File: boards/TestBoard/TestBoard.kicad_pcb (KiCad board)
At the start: 2 copper layers, 27 x 69 mm, 26 parts, among them J1 Conn_01x04, J10 Conn_01x02, J11 Conn_01x02, J2 Conn_01x04, J3 Conn_01x80, J4 Conn_01x02, J5 Conn_01x80, U1 MCP23017_ML, U2 MCP23017_ML, U3 MCP23017_ML, U4 MCP23017_ML, U5 MCP23017_ML

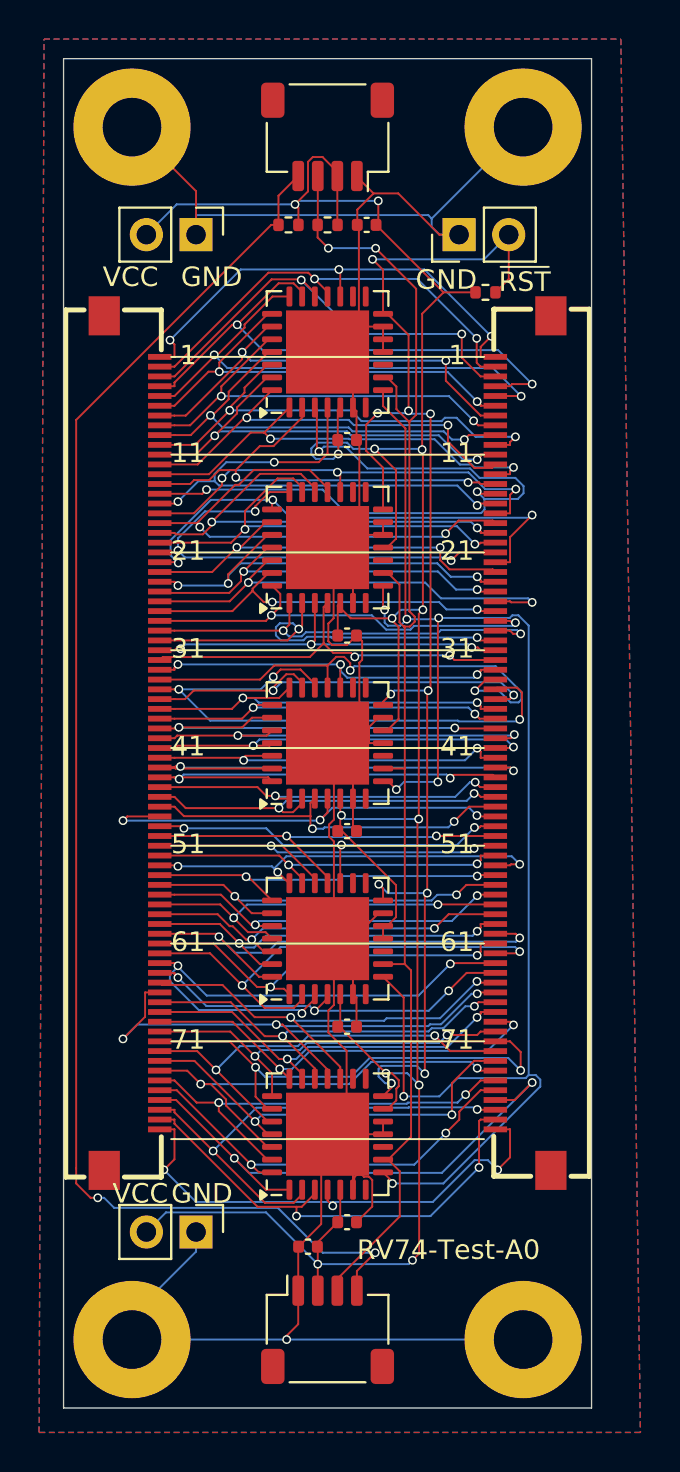
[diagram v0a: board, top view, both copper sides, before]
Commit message: Re-route with wider tracks and vias, to avoid "Danger" notifications from JLCPCB.
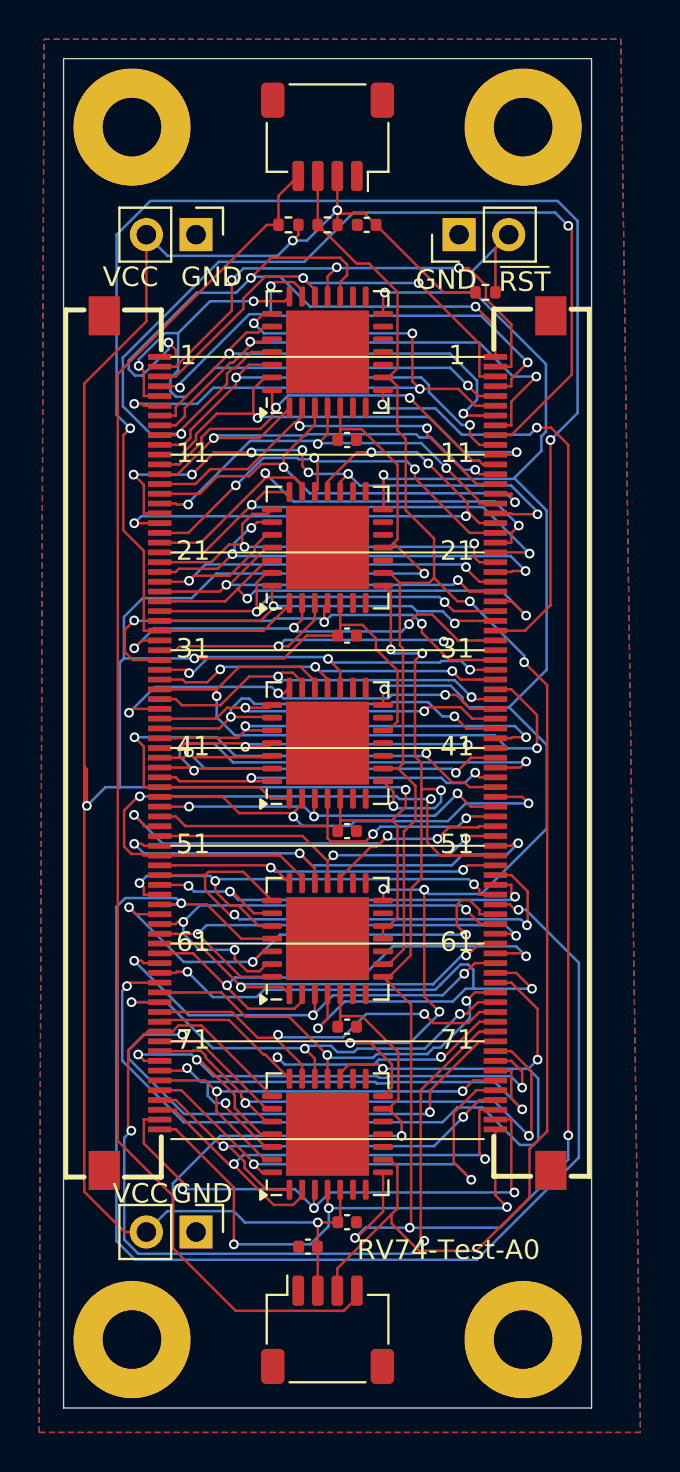
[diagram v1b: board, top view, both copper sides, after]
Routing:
- net GND: track 162.7 -> 0.00 mm, vias 1 -> 0
- net VCC: track 151.8 -> 207.9 mm, vias 13 -> 8
- net /A28: track 21.8 -> 77.5 mm
- net /A56: track 20.1 -> 70.0 mm
- net /A8: track 22.9 -> 53.0 mm
- net SDA: track 72.1 -> 101.2 mm
- net /A69: track 20.6 -> 48.0 mm
- net /A64: track 23.0 -> 49.5 mm, vias 2 -> 3
- net SCK: track 81.4 -> 106.6 mm, vias 7 -> 9
- net /A51: track 18.9 -> 34.0 mm
- net ~{RESET}: track 72.7 -> 87.6 mm, vias 10 -> 7
- net /A63: track 20.0 -> 34.3 mm
- net /A44: track 18.6 -> 30.2 mm
- net /A0: track 24.5 -> 35.6 mm
- net /A14: track 35.5 -> 24.6 mm, vias 3 -> 2
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
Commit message: Use larger vias. Auto-routing is still working !! That's good placement :)
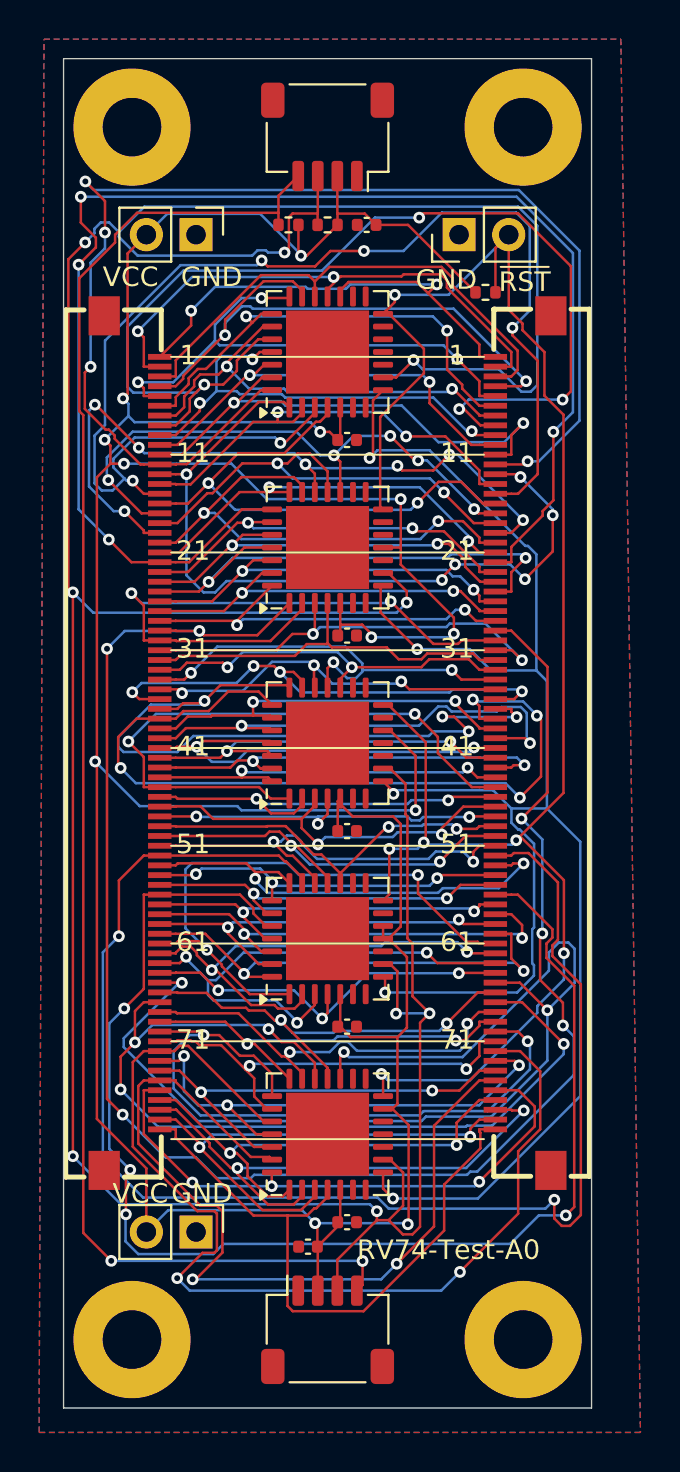
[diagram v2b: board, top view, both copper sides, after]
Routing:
- net SDA: track 101.2 -> 182.3 mm, vias 2 -> 9
- net /A21: track 21.3 -> 73.1 mm, vias 2 -> 4
- net /A56: track 70.0 -> 19.8 mm
- net /A55: track 24.6 -> 69.2 mm, vias 3 -> 4
- net /A11: track 21.4 -> 65.6 mm, vias 2 -> 4
- net /A14: track 24.6 -> 65.8 mm, vias 2 -> 5
- net /A51: track 34.0 -> 73.8 mm
- net /A7: track 27.1 -> 56.4 mm, vias 2 -> 4
- net /A8: track 53.0 -> 24.0 mm, vias 2 -> 3
- net /A71: track 28.4 -> 53.4 mm
- net /A37: track 19.2 -> 42.1 mm, vias 2 -> 4
- net /A66: track 24.0 -> 46.8 mm, vias 3 -> 4
- net /A74: track 22.5 -> 44.3 mm
- net /A12: track 23.4 -> 39.9 mm, vias 2 -> 6
- net /A36: track 22.2 -> 38.1 mm, vias 3 -> 4
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
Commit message: EVen larger vias and track clearance
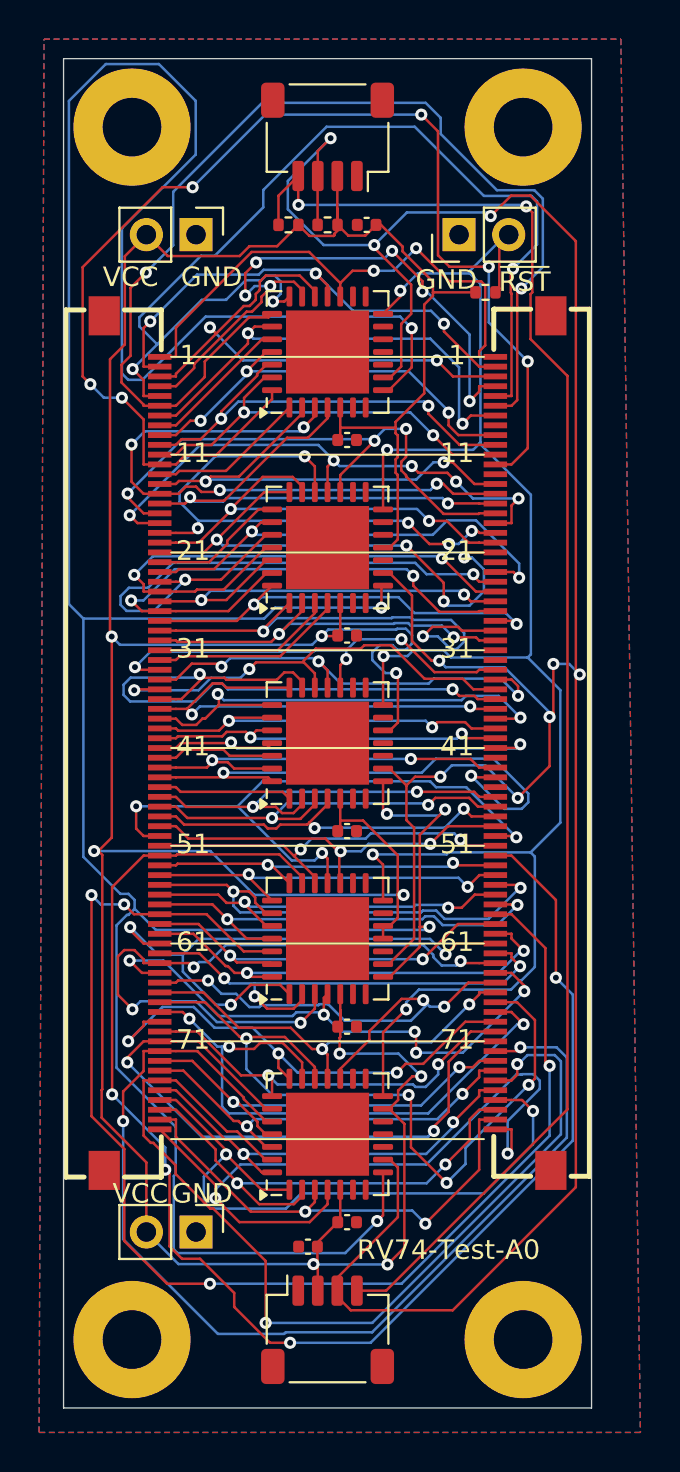
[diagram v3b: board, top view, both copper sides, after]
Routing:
- net SCK: track 94.3 -> 167.6 mm, vias 5 -> 6
- net /A21: track 73.1 -> 6.96 mm, vias 4 -> 0
- net /A28: track 89.3 -> 25.2 mm, vias 6 -> 2
- net /A55: track 69.2 -> 19.8 mm, vias 4 -> 2
- net /A7: track 56.4 -> 7.57 mm, vias 4 -> 0
- net /A57: track 23.2 -> 67.6 mm, vias 2 -> 4
- net /A14: track 65.8 -> 31.8 mm, vias 5 -> 4
- net SDA: track 182.3 -> 148.5 mm
- net /A5: track 24.5 -> 56.9 mm
- net /A12: track 39.9 -> 8.04 mm, vias 6 -> 0
- net /A64: track 56.2 -> 25.9 mm
- net /A4: track 27.6 -> 53.8 mm
- net /A44: track 31.7 -> 6.87 mm, vias 2 -> 0
- net /A37: track 42.1 -> 24.4 mm, vias 4 -> 2
- net /A36: track 38.1 -> 23.4 mm, vias 4 -> 2
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
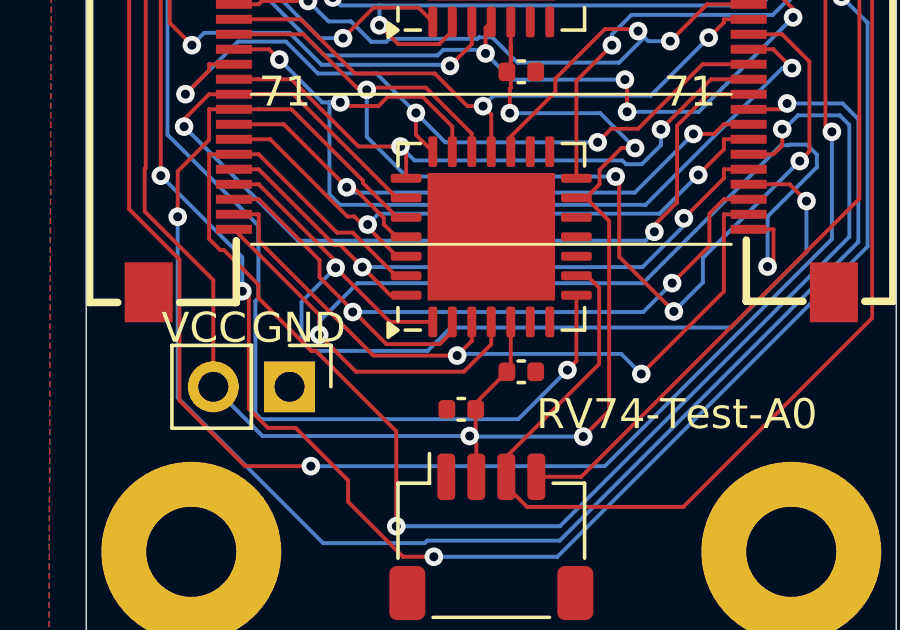
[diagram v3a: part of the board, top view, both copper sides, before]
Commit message: Rework one track to avoid solder-mask / pad clearance violation reported by JLCPCB DFM checker
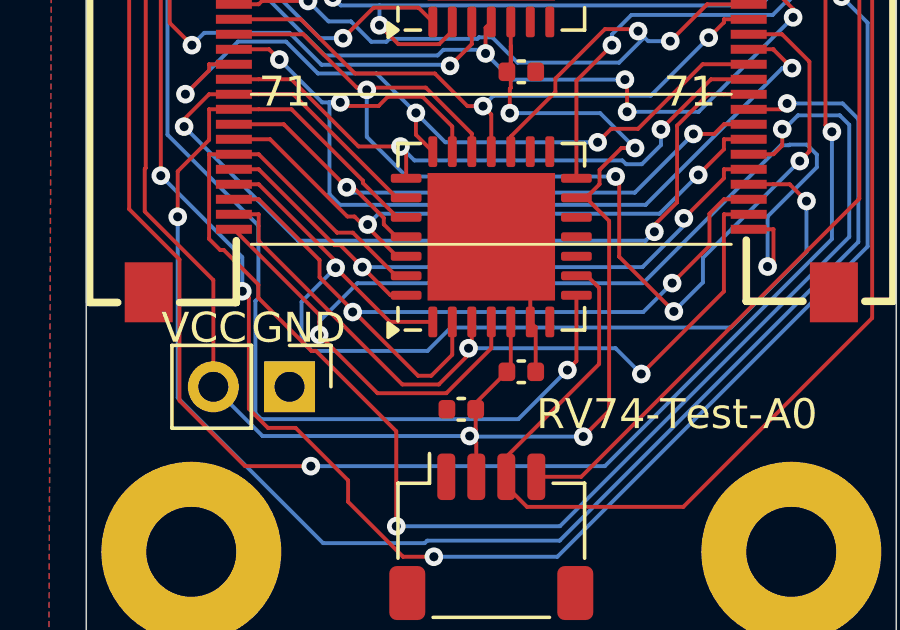
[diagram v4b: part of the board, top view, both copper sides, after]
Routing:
- net GND: track 0.00 -> 5.11 mm
- net /A77: track 25.5 -> 27.2 mm
- net /A78: track 25.0 -> 25.6 mm
- net /A79: track 38.2 -> 38.9 mm
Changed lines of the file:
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@@
 	)
 	(segment
+		(start 140.98 86.5175)
+		(end 140.8 86.3375)
+		(width 0.13)
+		(layer "F.Cu")
+		(net 1)
+	)
+	(segment
+		(start 140.8 86.3375)
+		(end 140.8 84.8)
+		(width 0.13)
+		(layer "F.Cu")
+		(net 1)
+	)
+	(segment
+		(start 140.98 88)
+		(end 140.98 86.5175)
+		(width 0.13)
+		(layer "F.Cu")
+		(net 1)
+	)
+	(segment
+		(start 140.8 84.8)
+		(end 139.5 83.5)
+		(width 0.13)
+		(layer "F.Cu")
+		(net 1)
+	)
+	(segment
 		(start 140.15 78.5357)
 		(end 140.1171 78.5686)
@@
 	)
 	(segment
-		(start 148.08 82.751)
-		(end 147.2533 82.751)
+		(start 136.5356 88.423)
+		(end 137.75 88.423)
 		(width 0.13)
 		(layer "F.Cu")
@@
 	)
 	(segment
-		(start 147.2533 85.3212)
+		(start 148.08 82.751)
 		(end 147.2533 82.751)
 		(width 0.13)
@@
 	)
 	(segment
-		(start 135.5716 87.459)
-		(end 138.3625 87.459)
+		(start 137.75 88.423)
+		(end 138.85 87.323)
 		(width 0.13)
 		(layer "F.Cu")
@@
 	)
 	(segment
-		(start 138.3625 87.459)
-		(end 138.85 86.9715)
+		(start 147.2533 85.3212)
+		(end 147.2533 82.751)
 		(width 0.13)
 		(layer "F.Cu")
@@
 	)
 	(segment
-		(start 131.7467 83.6341)
-		(end 135.5716 87.459)
+		(start 131.7467 82.75)
+		(end 131.7467 83.6341)
 		(width 0.13)
 		(layer "F.Cu")
@@
 	)
 	(segment
-		(start 131.7467 82.75)
-		(end 131.7467 83.6341)
+		(start 138.85 87.323)
+		(end 138.85 86.3375)
 		(width 0.13)
 		(layer "F.Cu")
@@
 	)
 	(segment
-		(start 138.85 86.9715)
-		(end 138.85 86.3375)
+		(start 131.7467 83.6341)
+		(end 136.5356 88.423)
 		(width 0.13)
 		(layer "F.Cu")
@@
 	)
 	(via
-		(at 138.3625 87.459)
+		(at 138.742197 87.215197)
 		(size 0.62)
 		(drill 0.3)
@@
 	)
 	(segment
-		(start 143.832 87.4045)
-		(end 144.501 88.0735)
-		(width 0.13)
-		(layer "B.Cu")
-		(net 23)
-	)
-	(segment
-		(start 138.417 87.4045)
-		(end 143.832 87.4045)
+		(start 144.501 88.0735)
+		(end 143.642697 87.215197)
 		(width 0.13)
 		(layer "B.Cu")
@@
 	)
 	(segment
-		(start 138.3625 87.459)
-		(end 138.417 87.4045)
+		(start 143.642697 87.215197)
+		(end 138.742197 87.215197)
 		(width 0.13)
 		(layer "B.Cu")
@@
 	)
 	(segment
-		(start 134.9904 87.9957)
-		(end 138.5849 87.9957)
+		(start 138 88.714)
+		(end 139.5 87.214)
 		(width 0.13)
 		(layer "F.Cu")
@@
 	)
 	(segment
-		(start 139.5 87.0806)
-		(end 139.5 86.3375)
-		(width 0.13)
-		(layer "F.Cu")
-		(net 25)
-	)
-	(segment
 		(start 133.7634 86.7687)
-		(end 134.9904 87.9957)
+		(end 135.7087 88.714)
 		(width 0.13)
 		(layer "F.Cu")
@@
 	)
 	(segment
-		(start 138.5849 87.9957)
-		(end 139.5 87.0806)
+		(start 135.7087 88.714)
+		(end 138 88.714)
 		(width 0.13)
 		(layer "F.Cu")
@@
 	)
 	(segment
+		(start 139.5 87.214)
+		(end 139.5 86.3375)
+		(width 0.13)
+		(layer "F.Cu")
+		(net 25)
+	)
+	(segment
 		(start 148.9067 84.2953)
 		(end 148.7101 84.4919)
@@
 	)
 	(segment
-		(start 134.9065 85.9805)
-		(end 136.003 87.077)
-		(width 0.13)
-		(layer "F.Cu")
-		(net 26)
-	)
-	(segment
 		(start 131.7467 82.25)
 		(end 133.7754 84.2787)
@@
 	)
 	(segment
+		(start 138.2 87.432)
+		(end 138.2 86.3375)
+		(width 0.13)
+		(layer "F.Cu")
+		(net 26)
+	)
+	(segment
 		(start 134.8793 86.0077)
 		(end 134.9065 85.9805)
@@
 	)
 	(segment
-		(start 137.7805 87.077)
-		(end 138.2 86.6575)
+		(start 137.5 88.132)
+		(end 138.2 87.432)
 		(width 0.13)
 		(layer "F.Cu")
@@
 	)
 	(segment
-		(start 130.92 82.25)
-		(end 131.7467 82.25)
+		(start 134.9065 85.9805)
+		(end 137.058 88.132)
 		(width 0.13)
 		(layer "F.Cu")
@@
 	)
 	(segment
-		(start 136.003 87.077)
-		(end 137.7805 87.077)
+		(start 130.92 82.25)
+		(end 131.7467 82.25)
 		(width 0.13)
 		(layer "F.Cu")
@@
 		(width 0.13)
 		(layer "F.Cu")
+		(net 26)
+	)
+	(segment
+		(start 137.058 88.132)
+		(end 137.5 88.132)
+		(width 0.13)
+		(layer "F.Cu")
